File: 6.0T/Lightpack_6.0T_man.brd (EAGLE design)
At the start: 78 x 78.1 mm, 31 parts, among them CN1 USB-MICRO-B, CN2 RJ11-5P-REEL-LIGHTPACK6T2, CN3 RJ11-5P-REEL-MAIN, IC1 AT90USB162, IC2 DM631_SOP24, IC3 DM631_SOP24, J1 DCJ0202, X1 16Mhz

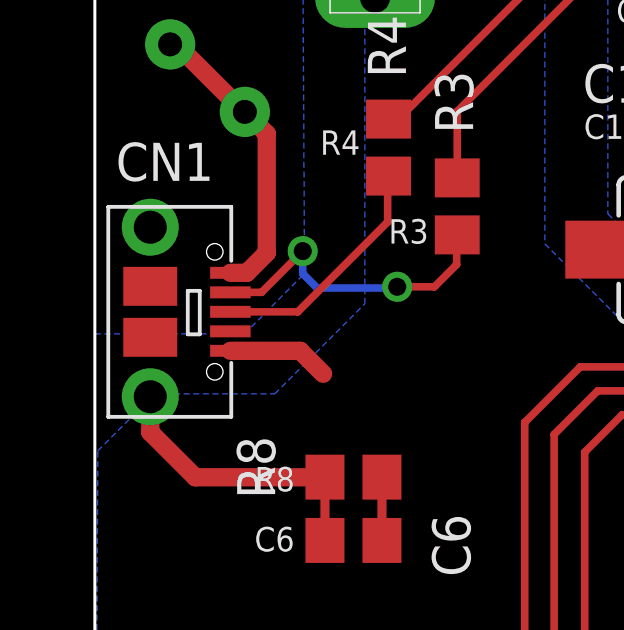
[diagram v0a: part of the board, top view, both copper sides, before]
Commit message: New universal microUSB footprint
*Some restriction added
*7 holes on milling (46) layer
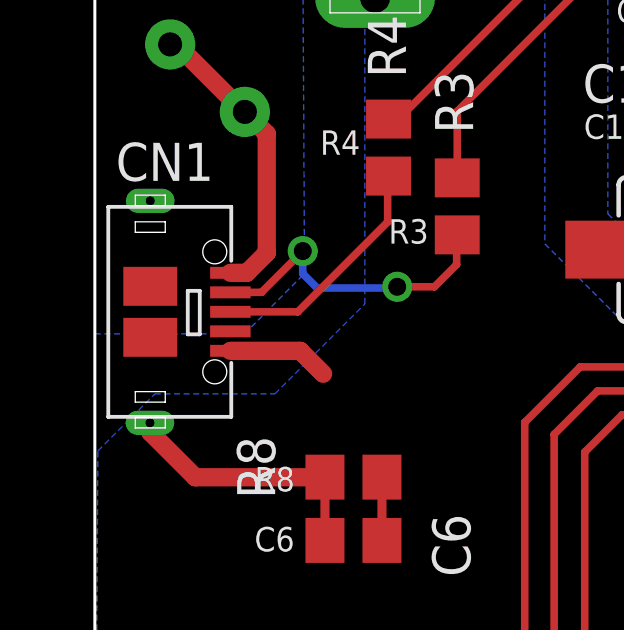
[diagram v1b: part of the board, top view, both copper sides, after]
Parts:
- CN1: value USB-MICRO-B -> USB-MICRO-B-UNIVERSAL; device _USB_sockets:USB-MICRO-B-5F -> _USB_sockets:USB-MICRO-B-UNIVERSAL
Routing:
- net N$44: track 9.98 -> 9.11 mm
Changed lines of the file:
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@@
 <layer number="2" name="Route2" color="1" fill="3" visible="no" active="no"/>
 <layer number="15" name="Route15" color="4" fill="6" visible="no" active="no"/>
-<layer number="16" name="Bottom" color="1" fill="1" visible="yes" active="yes"/>
+<layer number="16" name="Bottom" color="1" fill="1" visible="no" active="yes"/>
 <layer number="17" name="Pads" color="2" fill="1" visible="yes" active="yes"/>
 <layer number="18" name="Vias" color="2" fill="1" visible="yes" active="yes"/>
@@
 <text x="5.1" y="55.3" size="1.27" layer="21" font="vector">S1</text>
 <text x="0.7" y="30.1" size="1.27" layer="21" font="vector">CN1</text>
+<rectangle x1="0" y1="22.55" x2="3.73" y2="29" layer="41"/>
+<rectangle x1="0" y1="24" x2="4" y2="29" layer="42"/>
+<rectangle x1="4" y1="25" x2="6" y2="28" layer="42"/>
 </plain>
 <attributes>
@@
 <attribute name="VALUE" x="10.48" y="25.49" size="1.27" layer="27" rot="R90"/>
 </element>
-<element name="CN1" library="_USB_sockets" package="USB-MICRO-B-5F" value="USB-MICRO-B" x="4.5475" y="25.735" smashed="yes" rot="R270"/>
+<element name="CN1" library="_USB_sockets" package="USB-MICRO-B-UNIVERSAL" value="USB-MICRO-B-UNIVERSAL" x="4.5475" y="25.735" smashed="yes" rot="R270"/>
 <element name="C6" library="rcl" package="C0805" value="10nF/500V" x="8.62" y="18.115" smashed="yes" rot="R180">
 <attribute name="NAME" x="11.2475" y="18.9975" size="1.27" layer="25" rot="R270"/>
@@
 <wire x1="7.645" y1="20.25" x2="7.67" y2="20.225" width="0.4064" layer="1"/>
 <wire x1="7.525" y1="20.37" x2="7.67" y2="20.225" width="0.6096" layer="1"/>
-<wire x1="1.8475" y1="22.905" x2="1.8475" y2="21.7225" width="0.6096" layer="1"/>
+<wire x1="1.8375" y1="22.035" x2="1.8475" y2="21.7225" width="0.6096" layer="1"/>
 <wire x1="1.8475" y1="21.7225" x2="3.35" y2="20.22" width="0.6096" layer="1"/>
 <wire x1="3.35" y1="20.22" x2="7.665" y2="20.22" width="0.6096" layer="1"/>

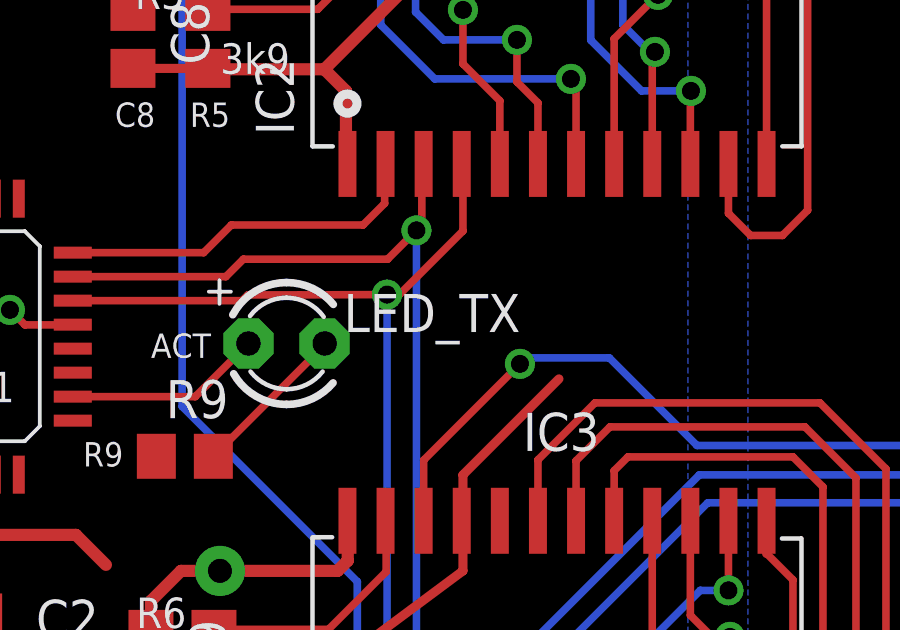
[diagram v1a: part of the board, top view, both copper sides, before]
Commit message: Fix names and R9 value
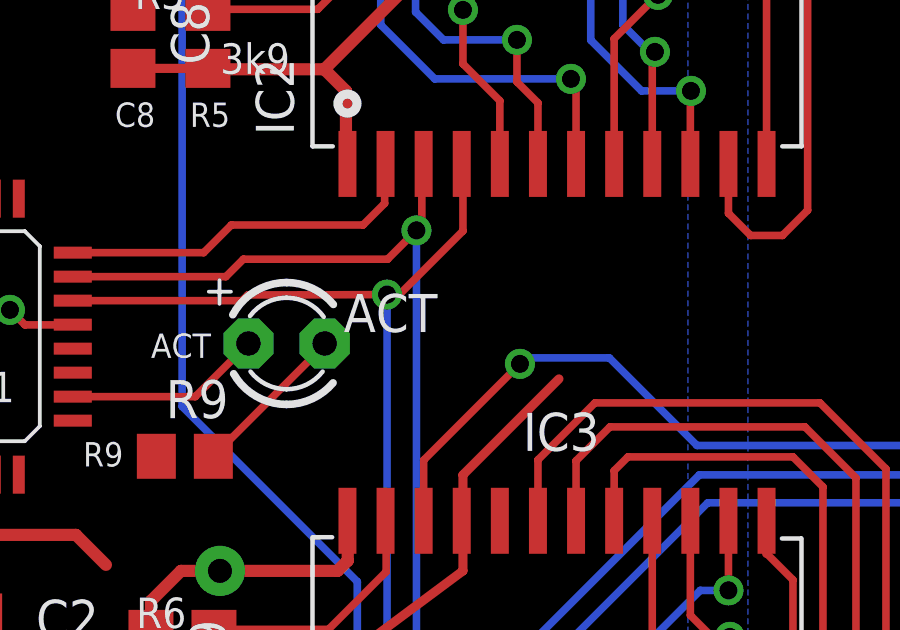
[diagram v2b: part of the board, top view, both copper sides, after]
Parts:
- R9: value 1k -> 249R
- renumbered LED_TX to ACT
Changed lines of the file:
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@@
 <layer number="2" name="Route2" color="1" fill="3" visible="no" active="no"/>
 <layer number="15" name="Route15" color="4" fill="6" visible="no" active="no"/>
-<layer number="16" name="Bottom" color="1" fill="1" visible="no" active="yes"/>
+<layer number="16" name="Bottom" color="1" fill="1" visible="yes" active="yes"/>
 <layer number="17" name="Pads" color="2" fill="1" visible="yes" active="yes"/>
 <layer number="18" name="Vias" color="2" fill="1" visible="yes" active="yes"/>
@@
 <element name="C9" library="rcl" package="C0805" value="100nF" x="33.1" y="30.4" rot="R270"/>
 <element name="D2" library="diode" package="SMB" value="SS14" x="30.9" y="63.3" rot="R270"/>
-<element name="LED_TX" library="adafruit" package="LED3MM" value="GREEN" x="37.62" y="40.88"/>
-<element name="R9" library="rcl" package="R0805" value="1k" x="34.23" y="37.12"/>
+<element name="ACT" library="adafruit" package="LED3MM" value="GREEN" x="37.62" y="40.88"/>
+<element name="R9" library="rcl" package="R0805" value="249R" x="34.23" y="37.12"/>
 <element name="C3" library="rcl" package="C0805" value="100nF" x="19.75" y="35.8" rot="R270"/>
 <element name="EXP_BOARD" library="brd-conn" package="MA05-1" value="" x="73.4" y="41.1" smashed="yes" rot="R90">
@@
 <signal name="N$37">
 <contactref element="R9" pad="2"/>
-<contactref element="LED_TX" pad="K"/>
+<contactref element="ACT" pad="K"/>
 <wire x1="38.89" y1="40.88" x2="38.89" y2="40.83" width="0.254" layer="1"/>
 <wire x1="38.89" y1="40.83" x2="35.18" y2="37.12" width="0.254" layer="1"/>
@@
 </signal>
 <signal name="N$3">
-<contactref element="LED_TX" pad="A"/>
+<contactref element="ACT" pad="A"/>
 <contactref element="IC1" pad="10"/>
 <wire x1="30.495" y1="39.1075" x2="34.5775" y2="39.1075" width="0.254" layer="1"/>

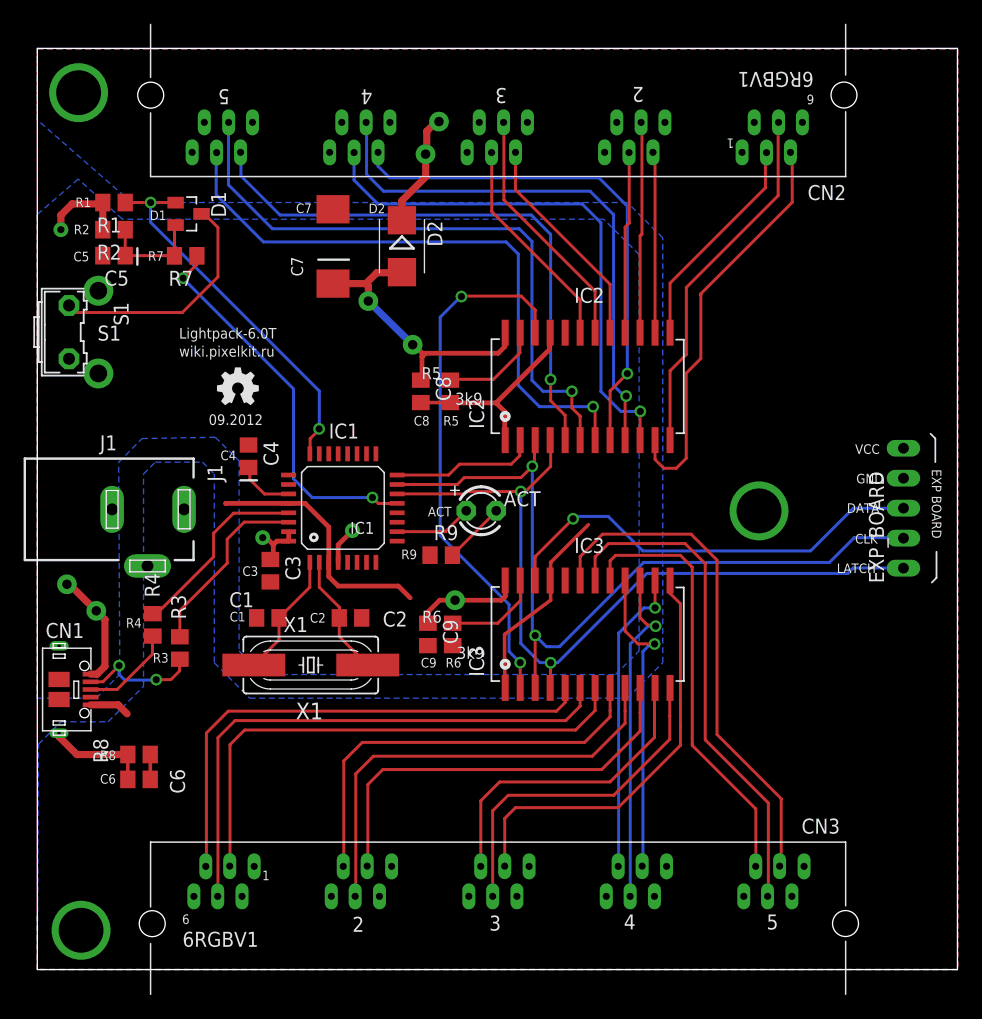
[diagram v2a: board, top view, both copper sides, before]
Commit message: Draft-angle enclosure type optimization
* tPlace silk updated (url, year)
* CN2, CN3 moved toward PCB center for 1mm
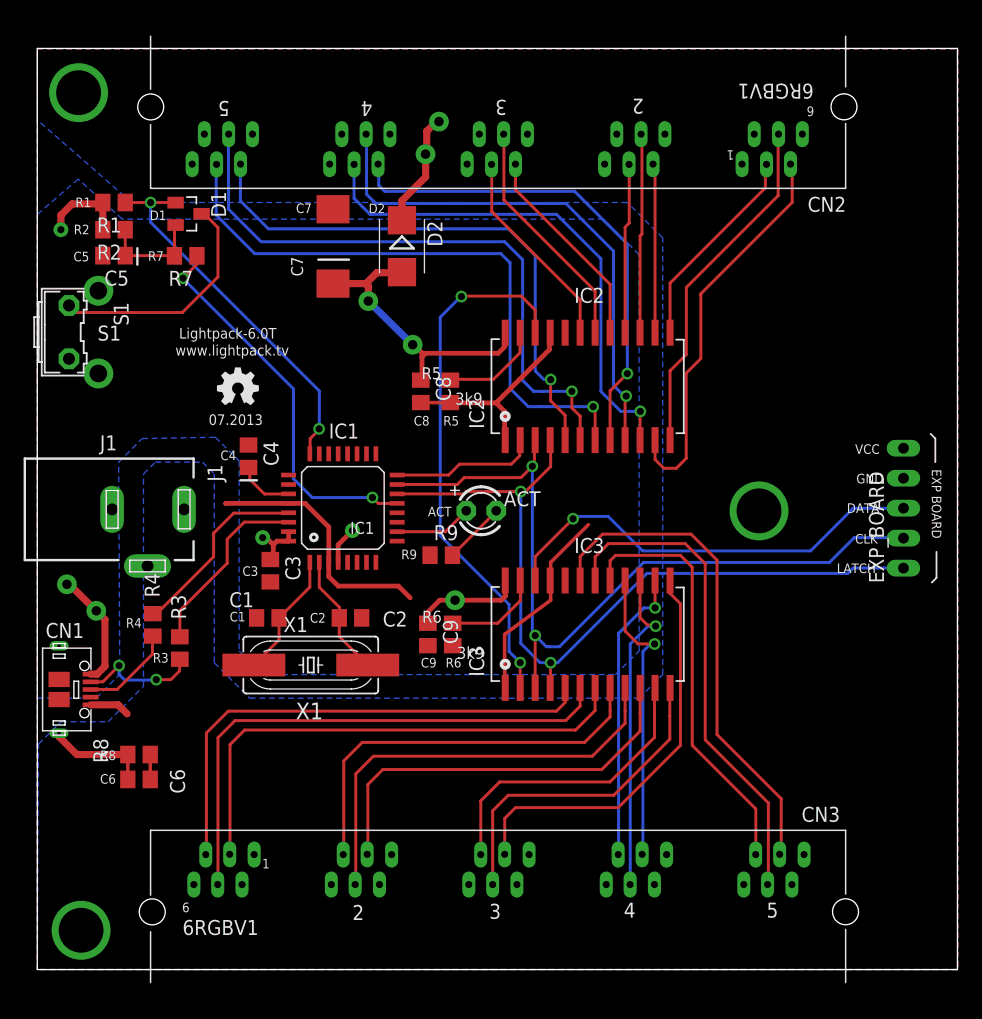
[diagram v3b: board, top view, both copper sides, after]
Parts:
- moved CN2 1.00 mm to (40.0, 72.8)
- moved CN3 1.00 mm to (38.1, 9.20)
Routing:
- net N$9: track 44.1 -> 42.2 mm
- net N$11: track 45.8 -> 43.9 mm
- net N$10: track 46.5 -> 44.6 mm
- net N$5: track 48.3 -> 47.1 mm
- net N$28: track 26.7 -> 25.7 mm
- net N$43: track 43.6 -> 42.6 mm
- net N$42: track 42.9 -> 41.9 mm
- net N$41: track 36.8 -> 35.8 mm
- net N$40: track 18.4 -> 17.4 mm
- net N$39: track 21.0 -> 20.0 mm
- net N$38: track 18.6 -> 17.6 mm
- net N$30: track 15.4 -> 14.4 mm
- net N$29: track 17.9 -> 16.9 mm
- net N$27: track 28.9 -> 27.9 mm
- net N$26: track 35.8 -> 34.8 mm
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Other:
- board text added: "07.2013"
- board text added: "www.lightpack.tv"
- board text removed: "09.2012"
- board text removed: "wiki.pixelkit.ru"

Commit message: tSilk + new microUSB socket + CN2,CN3 moving (see details)
-- P/N + ID on tSilk
-- Slots of mUSB increased to 1.0x0.5mm
-- New solid rect in mUSB component (commited in Pixelkit lib) named EVT
-- CN2,3 moved on 0.1mm out of center
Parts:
- CN1: value USB-MICRO-B-UNIVERSAL -> USB-MICRO-B-EVT; device _USB_sockets:USB-MICRO-B-UNIVERSAL -> _USB_sockets:USB-MICRO-B-UNIVERSAL-SOLID-FOOTS
- moved CN2 0.20 mm to (40.1, 73.0)
- moved CN3 0.16 mm to (38.1, 9.05)
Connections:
- net N$44: now also CN1.P$1; no longer CN1.P$7
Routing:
- net N$44: track 9.11 -> 12.8 mm
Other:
- board text added: "08.2013"
- board text added: "ED12C5X06-A0"
- board text added: "P/N: EPB0012330"
- board text removed: "07.2013"

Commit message: update microUSB foots for EVT (see EAGLE-libs commit)
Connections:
- net N$44: now also CN1.P$4; no longer CN1.P$1
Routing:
- net N$44: track 12.8 -> 9.56 mm
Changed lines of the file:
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@@
 </signal>
 <signal name="N$33">
-<contactref element="CN1" pad="D+"/>
+<contactref element="CN1" pad="D+" route="any" routetag="D+"/>
 <contactref element="R4" pad="1"/>
 <wire x1="4.5175" y1="25.735" x2="6.765" y2="25.735" width="0.254" layer="1"/>
@@
 <contactref element="C6" pad="2"/>
 <wire x1="7.67" y1="20.225" x2="7.67" y2="18.115" width="0.3048" layer="1"/>
-<contactref element="CN1" pad="P$1"/>
+<contactref element="CN1" pad="P$4" route="any" routetag="SHIELD1"/>
 <wire x1="7.645" y1="20.25" x2="7.67" y2="20.225" width="0.4064" layer="1"/>
 <wire x1="7.525" y1="20.37" x2="7.67" y2="20.225" width="0.6096" layer="1"/>
-<wire x1="1.8475" y1="25.735" x2="1.8475" y2="21.7225" width="0.6096" layer="1"/>
+<wire x1="1.8475" y1="22.485" x2="1.8475" y2="21.7225" width="0.6096" layer="1"/>
 <wire x1="1.8475" y1="21.7225" x2="3.35" y2="20.22" width="0.6096" layer="1"/>
 <wire x1="3.35" y1="20.22" x2="7.665" y2="20.22" width="0.6096" layer="1"/>
